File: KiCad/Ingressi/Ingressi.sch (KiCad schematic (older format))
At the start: 4 parts, among them J1 NL4MP-M3, J2 NL4MP-M3, J3 Faston, J4 XXXX

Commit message: schematic finished
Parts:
- removed J1, J2: NL4MP-M3, symbol Connector:Conn_01x04_Female
- added J1, J2: SpeakON_NL4, Connector Audio:Jack_speakON_Neutrik_NL4MP, symbol Connector:SpeakON_NL4
- J3: value Faston -> Phoenix MKDS; footprint (none) -> Connector Phoenix MSTB:PhoenixContact_MKDS_5_1x04_P6.35mm
- J4: value XXXX -> JST_S4P-VH; footprint (none) -> Connector JST:JST_VH_S4P-VH_1x04_P3.96mm_Horizontal
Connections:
- net 1+: no longer names the net of J3.1 (Pin_1), J4.1 (Pin_1)
- net 1+: now also J1.1+, J2.1+
- net 1-: no longer names the net of J3.2 (Pin_2), J4.2 (Pin_2)
- net 1-: now also J1.1-, J2.1-
- net 2+: no longer names the net of J3.3 (Pin_3), J4.3 (Pin_3)
- net 2+: now also J1.2+, J2.2+
- net 2-: no longer names the net of J3.4 (Pin_4), J4.4 (Pin_4)
- net 2-: now also J1.2-, J2.2-
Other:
- moved on the sheet: J3, J4
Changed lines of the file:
@@
 $EndDescr
 $Comp
-L Connector:Conn_01x04_Female J2
-U 1 1 5FD230A4
-P 6350 3650
-F 0 "J2" H 6378 3626 50  0000 L CNN
-F 1 "NL4MP-M3" H 6378 3535 50  0000 L CNN
-F 2 "" H 6350 3650 50  0001 C CNN
-F 3 "~" H 6350 3650 50  0001 C CNN
-	1    6350 3650
+L Connector:SpeakON_NL4 J1
+U 1 1 5FD43F0D
+P 4750 3650
+F 0 "J1" H 4750 4131 50  0000 C CNN
+F 1 "SpeakON_NL4" H 4750 4040 50  0000 C CNN
+F 2 "Connector Audio:Jack_speakON_Neutrik_NL4MP" H 4750 3650 50  0001 C CNN
+F 3 "http://www.neutrik.com/en/speakon/" H 4750 3650 50  0001 C CNN
+	1    4750 3650
 	1    0    0    -1
 $EndComp
+Wire Wire Line
+	4750 3350 5250 3350
+Wire Wire Line
+	4750 3950 5450 3950
+Wire Wire Line
+	6700 3650 6700 4200
+Wire Wire Line
+	6700 4200 6300 4200
+Wire Wire Line
+	4450 4200 4450 3650
+Wire Wire Line
+	5050 3650 5050 4450
+Wire Wire Line
+	5050 4450 5550 4450
+Wire Wire Line
+	7300 4450 7300 3650
+Wire Wire Line
+	5250 4750 5250 3350
+Connection ~ 5250 3350
+Wire Wire Line
+	5250 3350 6200 3350
+Wire Wire Line
+	5350 4750 5350 4200
+Connection ~ 5350 4200
+Wire Wire Line
+	5350 4200 4450 4200
+Wire Wire Line
+	6200 4750 6200 3350
+Connection ~ 6200 3350
+Wire Wire Line
+	6200 3350 7000 3350
+Wire Wire Line
+	6300 4750 6300 4200
+Connection ~ 6300 4200
+Wire Wire Line
+	6300 4200 5350 4200
+Wire Wire Line
+	5450 4750 5450 3950
+Connection ~ 5450 3950
+Wire Wire Line
+	5450 3950 6400 3950
+Wire Wire Line
+	5550 4750 5550 4450
+Connection ~ 5550 4450
+Wire Wire Line
+	5550 4450 6500 4450
+Wire Wire Line
+	6400 4750 6400 3950
+Connection ~ 6400 3950
+Wire Wire Line
+	6400 3950 7000 3950
+Wire Wire Line
+	6500 4750 6500 4450
+Connection ~ 6500 4450
+Wire Wire Line
+	6500 4450 7300 4450
 $Comp
-L Connector:Conn_01x04_Female J1
-U 1 1 5FD256AD
-P 4850 3650
-F 0 "J1" H 4950 3650 50  0000 C CNN
-F 1 "NL4MP-M3" H 5100 3550 50  0000 C CNN
-F 2 "" H 4850 3650 50  0001 C CNN
-F 3 "~" H 4850 3650 50  0001 C CNN
-	1    4850 3650
-	-1   0    0    -1
+L Connector:SpeakON_NL4 J2
+U 1 1 5FD48C19
+P 7000 3650
+F 0 "J2" H 7000 4131 50  0000 C CNN
+F 1 "SpeakON_NL4" H 7000 4040 50  0000 C CNN
+F 2 "Connector Audio:Jack_speakON_Neutrik_NL4MP" H 7000 3650 50  0001 C CNN
+F 3 "http://www.neutrik.com/en/speakon/" H 7000 3650 50  0001 C CNN
+	1    7000 3650
+	1    0    0    -1
 $EndComp
 $Comp
 L Connector:Conn_01x04_Female J3
 U 1 1 5FD26AE9
-P 5250 4450
-F 0 "J3" V 5350 4350 50  0000 L CNN
-F 1 "Faston" V 5450 4250 50  0000 L CNN
-F 2 "" H 5250 4450 50  0001 C CNN
-F 3 "~" H 5250 4450 50  0001 C CNN
-	1    5250 4450
+P 5350 4950
+F 0 "J3" V 5200 5150 50  0000 L CNN
+F 1 "Phoenix MKDS" V 5300 5150 50  0000 L CNN
+F 2 "Connector Phoenix MSTB:PhoenixContact_MKDS_5_1x04_P6.35mm" H 5350 4950 50  0001 C CNN
+F 3 "~" H 5350 4950 50  0001 C CNN
+	1    5350 4950
 	0    -1   1    0
 $EndComp
@@
 L Connector:Conn_01x04_Female J4
 U 1 1 5FD27467
-P 5750 4450
-F 0 "J4" V 5850 4450 50  0000 R CNN
-F 1 "XXXX" V 5950 4500 50  0000 R CNN
-F 2 "" H 5750 4450 50  0001 C CNN
-F 3 "~" H 5750 4450 50  0001 C CNN
-	1    5750 4450
+P 6300 4950
+F 0 "J4" V 6146 4662 50  0000 R CNN
+F 1 "JST_S4P-VH" V 6237 4662 50  0000 R CNN
+F 2 "Connector JST:JST_VH_S4P-VH_1x04_P3.96mm_Horizontal" H 6300 4950 50  0001 C CNN
+F 3 "~" H 6300 4950 50  0001 C CNN
+	1    6300 4950
 	0    -1   1    0
 $EndComp
-Wire Wire Line
-	5050 3550 5150 3550
-Wire Wire Line
-	5050 3650 5250 3650
-Wire Wire Line
-	5050 3750 5350 3750
-Wire Wire Line
-	5050 3850 5450 3850
-Wire Wire Line
-	5150 4250 5150 3550
-Connection ~ 5150 3550
-Wire Wire Line
-	5150 3550 5650 3550
-Wire Wire Line
-	5250 4250 5250 3650
-Connection ~ 5250 3650
-Wire Wire Line
-	5250 3650 5750 3650
-Wire Wire Line
-	5350 4250 5350 3750
-Connection ~ 5350 3750
-Wire Wire Line
-	5350 3750 5850 3750
-Wire Wire Line
-	5450 4250 5450 3850
-Connection ~ 5450 3850
-Wire Wire Line
-	5450 3850 5950 3850
-Wire Wire Line
-	5650 4250 5650 3550
-Connection ~ 5650 3550
-Wire Wire Line
-	5650 3550 6150 3550
-Wire Wire Line
-	5750 4250 5750 3650
-Connection ~ 5750 3650
-Wire Wire Line
-	5750 3650 6150 3650
-Wire Wire Line
-	5850 4250 5850 3750
-Connection ~ 5850 3750
-Wire Wire Line
-	5850 3750 6150 3750
-Wire Wire Line
-	5950 4250 5950 3850
-Connection ~ 5950 3850
-Wire Wire Line
-	5950 3850 6150 3850
-Text Label 5500 3550 0    50   ~ 0
-1+
-Text Label 5500 3650 0    50   ~ 0
-1-
-Text Label 5500 3750 0    50   ~ 0
-2+
-Text Label 5500 3850 0    50   ~ 0
-2-
 $EndSCHEMATC

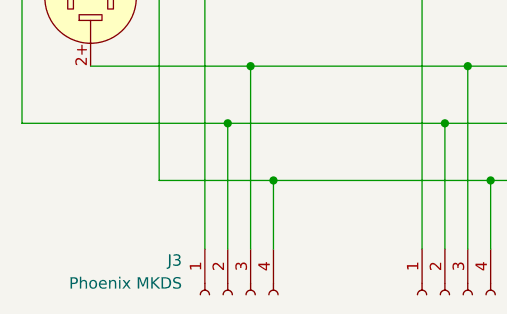
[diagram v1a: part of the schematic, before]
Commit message: Phoenix connector updated and added gerbers
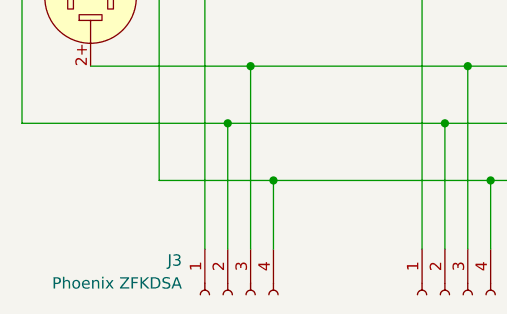
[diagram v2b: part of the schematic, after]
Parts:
- J3: value Phoenix MKDS -> Phoenix ZFKDSA; footprint Connector Phoenix MSTB:PhoenixContact_MKDS_5_1x04_P6.35mm -> Test:Phoenix_ZFKDSA_2,5_5,08_4
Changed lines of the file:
@@
 P 5350 4950
 F 0 "J3" V 5200 5150 50  0000 L CNN
-F 1 "Phoenix MKDS" V 5300 5150 50  0000 L CNN
-F 2 "Connector Phoenix MSTB:PhoenixContact_MKDS_5_1x04_P6.35mm" H 5350 4950 50  0001 C CNN
+F 1 "Phoenix ZFKDSA" V 5300 5150 50  0000 L CNN
+F 2 "Test:Phoenix_ZFKDSA_2,5_5,08_4" H 5350 4950 50  0001 C CNN
 F 3 "~" H 5350 4950 50  0001 C CNN
 	1    5350 4950

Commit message: changed JST
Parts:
- J4: footprint Connector JST:JST_VH_S4P-VH_1x04_P3.96mm_Horizontal -> Connector_JST:JST_VH_B4PS-VH_1x04_P3.96mm_Horizontal
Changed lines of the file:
@@
 F 0 "J4" V 6146 4662 50  0000 R CNN
 F 1 "JST_S4P-VH" V 6237 4662 50  0000 R CNN
-F 2 "Connector JST:JST_VH_S4P-VH_1x04_P3.96mm_Horizontal" H 6300 4950 50  0001 C CNN
+F 2 "Connector_JST:JST_VH_B4PS-VH_1x04_P3.96mm_Horizontal" H 6300 4950 50  0001 C CNN
 F 3 "~" H 6300 4950 50  0001 C CNN
 	1    6300 4950

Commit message: schematic updated
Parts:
- J3: value Phoenix ZFKDSA -> Phoenix
- J4: value JST_S4P-VH -> JST
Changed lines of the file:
@@
 P 5350 4950
 F 0 "J3" V 5200 5150 50  0000 L CNN
-F 1 "Phoenix ZFKDSA" V 5300 5150 50  0000 L CNN
+F 1 "Phoenix" V 5300 5150 50  0000 L CNN
 F 2 "Test:Phoenix_ZFKDSA_2,5_5,08_4" H 5350 4950 50  0001 C CNN
 F 3 "~" H 5350 4950 50  0001 C CNN
@@
 P 6300 4950
 F 0 "J4" V 6146 4662 50  0000 R CNN
-F 1 "JST_S4P-VH" V 6237 4662 50  0000 R CNN
+F 1 "JST" V 6237 4662 50  0000 R CNN
 F 2 "Connector_JST:JST_VH_B4PS-VH_1x04_P3.96mm_Horizontal" H 6300 4950 50  0001 C CNN
 F 3 "~" H 6300 4950 50  0001 C CNN

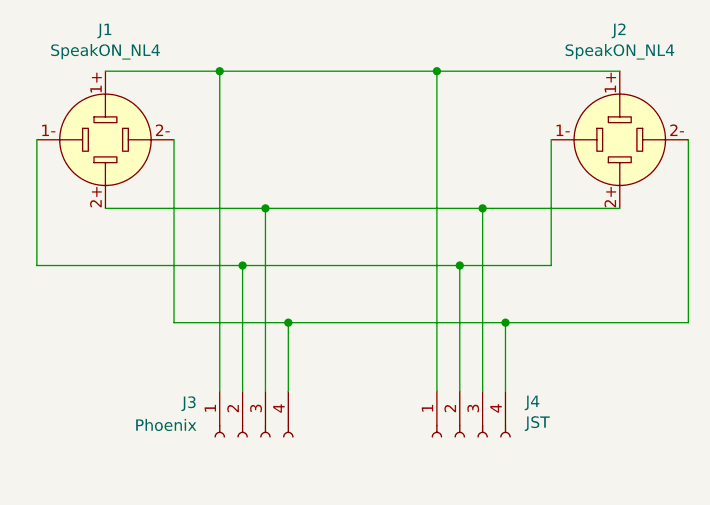
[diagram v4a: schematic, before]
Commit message: added faston connector
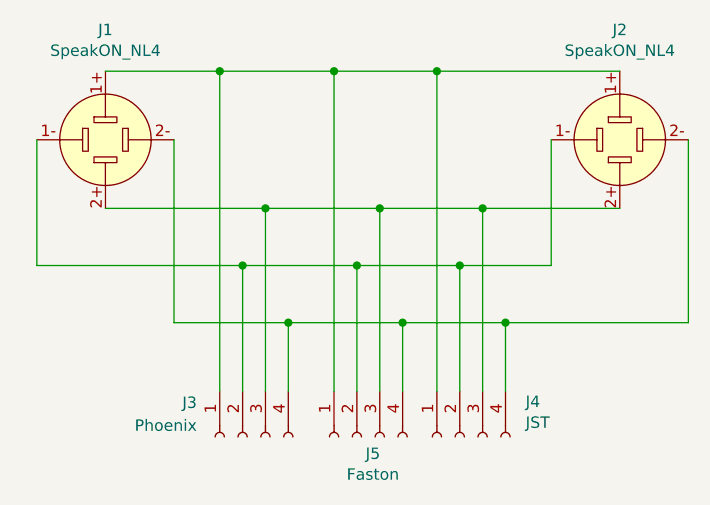
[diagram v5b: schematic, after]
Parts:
- added J5: Faston, Ingressi:Faston_01x04_P5.08mm_D5.08mm, symbol Connector:Conn_01x04_Female
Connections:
- net at J1.1+, J2.1+, J3.1 (Pin_1)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: now also J5.1 (Pin_1)
- net at J1.1-, J2.1-, J3.2 (Pin_2)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: now also J5.2 (Pin_2)
- net at J1.2+, J2.2+, J3.3 (Pin_3)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: now also J5.3 (Pin_3)
- net at J1.2-, J2.2-, J3.4 (Pin_4)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: now also J5.4 (Pin_4)
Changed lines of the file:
@@
 Connection ~ 5250 3350
 Wire Wire Line
-	5250 3350 6200 3350
+	5250 3350 5750 3350
 Wire Wire Line
 	5350 4750 5350 4200
@@
 Connection ~ 6300 4200
 Wire Wire Line
-	6300 4200 5350 4200
+	6300 4200 5850 4200
 Wire Wire Line
 	5450 4750 5450 3950
 Connection ~ 5450 3950
 Wire Wire Line
-	5450 3950 6400 3950
+	5450 3950 5950 3950
 Wire Wire Line
 	5550 4750 5550 4450
 Connection ~ 5550 4450
 Wire Wire Line
-	5550 4450 6500 4450
+	5550 4450 6050 4450
 Wire Wire Line
 	6400 4750 6400 3950
@@
 	0    -1   1    0
 $EndComp
+$Comp
+L Connector:Conn_01x04_Female J5
+U 1 1 60DB1C95
+P 5850 4950
+F 0 "J5" V 5923 4880 50  0000 C CNN
+F 1 "Faston" V 6014 4880 50  0000 C CNN
+F 2 "Ingressi:Faston_01x04_P5.08mm_D5.08mm" H 5850 4950 50  0001 C CNN
+F 3 "~" H 5850 4950 50  0001 C CNN
+	1    5850 4950
+	0    -1   1    0
+$EndComp
+Wire Wire Line
+	5750 4750 5750 3350
+Connection ~ 5750 3350
+Wire Wire Line
+	5750 3350 6200 3350
+Wire Wire Line
+	5850 4750 5850 4200
+Connection ~ 5850 4200
+Wire Wire Line
+	5850 4200 5350 4200
+Wire Wire Line
+	5950 4750 5950 3950
+Connection ~ 5950 3950
+Wire Wire Line
+	5950 3950 6400 3950
+Wire Wire Line
+	6050 4750 6050 4450
+Connection ~ 6050 4450
+Wire Wire Line
+	6050 4450 6500 4450
 $EndSCHEMATC
